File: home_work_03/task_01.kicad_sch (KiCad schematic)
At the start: 29 parts

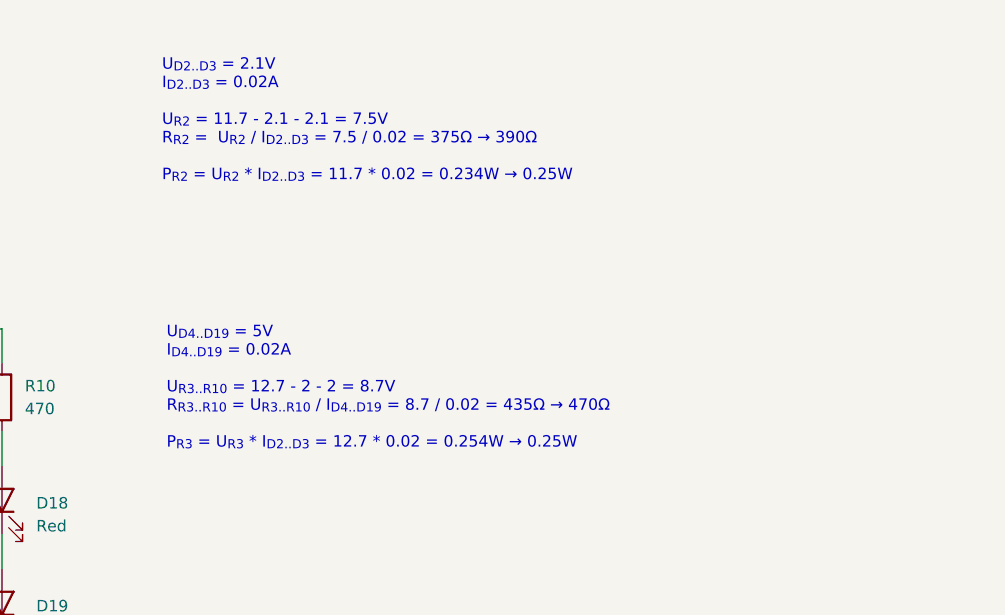
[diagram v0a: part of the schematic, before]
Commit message: fix home work 3
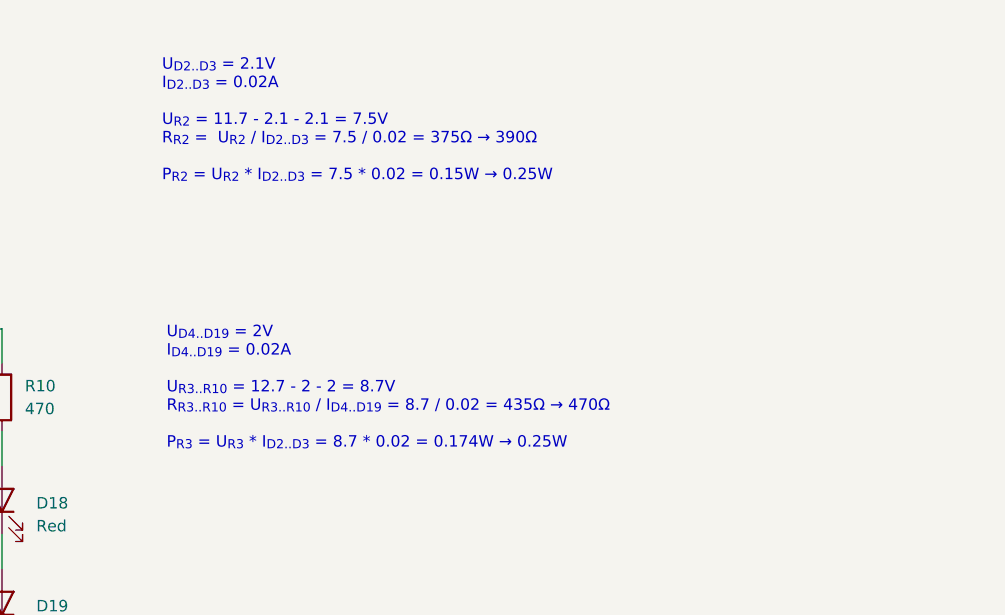
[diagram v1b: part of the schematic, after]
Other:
- note added: "U_{D2..D3} = 2.1V I_{D2..D3} = 0.02A U_{R2} = 11.7 - 2.1 - 2.1 = 7.5V R_{R2} = U_{R2} / I_{D2..D3} = 7.5 / 0.02 = 375Ω → 390Ω P_{R2} = U_{R2} * I_{D2..D3} = 7.5 * 0.02 = 0.15W → 0.25W"
- note added: "U_{D4..D19} = 2V I_{D4..D19} = 0.02A U_{R3..R10} = 12.7 - 2 - 2 = 8.7V R_{R3..R10} = U_{R3..R10} / I_{D4..D19} = 8.7 / 0.02 = 435Ω → 470Ω P_{R3} = U_{R3} * I_{D2..D3} = 8.7 * 0.02 = 0.174W → 0.25W"
- note removed: "U_{D2..D3} = 2.1V I_{D2..D3} = 0.02A U_{R2} = 11.7 - 2.1 - 2.1 = 7.5V R_{R2} = U_{R2} / I_{D2..D3} = 7.5 / 0.02 = 375Ω → 390Ω P_{R2} = U_{R2} * I_{D2..D3} = 11.7 * 0.02 = 0.234W → 0.25W"
- note removed: "U_{D4..D19} = 5V I_{D4..D19} = 0.02A U_{R3..R10} = 12.7 - 2 - 2 = 8.7V R_{R3..R10} = U_{R3..R10} / I_{D4..D19} = 8.7 / 0.02 = 435Ω → 470Ω P_{R3} = U_{R3} * I_{D2..D3} = 12.7 * 0.02 = 0.254W → 0.25W"
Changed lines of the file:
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@@
 		)
 	)
-	(text "U_{D2..D3} = 2.1V\nI_{D2..D3} = 0.02A\n\nU_{R2} = 11.7 - 2.1 - 2.1 = 7.5V\nR_{R2} =  U_{R2} / I_{D2..D3} = 7.5 / 0.02 = 375Ω → 390Ω\n\nP_{R2} = U_{R2} * I_{D2..D3} = 11.7 * 0.02 = 0.234W → 0.25W"
+	(text "U_{D2..D3} = 2.1V\nI_{D2..D3} = 0.02A\n\nU_{R2} = 11.7 - 2.1 - 2.1 = 7.5V\nR_{R2} =  U_{R2} / I_{D2..D3} = 7.5 / 0.02 = 375Ω → 390Ω\n\nP_{R2} = U_{R2} * I_{D2..D3} = 7.5 * 0.02 = 0.15W → 0.25W"
 		(exclude_from_sim no)
 		(at 119.38 74.676 0)
@@
 		)
 	)
-	(text "U_{D4..D19} = 5V\nI_{D4..D19} = 0.02A\n\nU_{R3..R10} = 12.7 - 2 - 2 = 8.7V\nR_{R3..R10} = U_{R3..R10} / I_{D4..D19} = 8.7 / 0.02 = 435Ω → 470Ω\n\nP_{R3} = U_{R3} * I_{D2..D3} = 12.7 * 0.02 = 0.254W → 0.25W"
+	(text "U_{D4..D19} = 2V\nI_{D4..D19} = 0.02A\n\nU_{R3..R10} = 12.7 - 2 - 2 = 8.7V\nR_{R3..R10} = U_{R3..R10} / I_{D4..D19} = 8.7 / 0.02 = 435Ω → 470Ω\n\nP_{R3} = U_{R3} * I_{D2..D3} = 8.7 * 0.02 = 0.174W → 0.25W"
 		(exclude_from_sim no)
 		(at 119.888 104.394 0)

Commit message: fix home work 03
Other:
- note added: "U_{D1} = 3.2V I_{D1} = 0.02A U_{R1} = 7.4 - 3.2 = 4.2V R_{R1} = U_{R1} / I_{D1} = 4.2 / 0.02 = 210Ω → 220Ω P_{R1} = U_{R1} * I_{D1} = 4.2 * 0.02 = 0.084W → 0.125W или 0603"
- note removed: "U_{D1} = 3.2V I_{D1} = 0.05A U_{R1} = 7.4 - 3.2 = 4.2V R_{R1} = U_{R1} / I_{D1} = 4.2 / 0.02 = 210Ω → 220Ω P_{R1} = U_{R1} * I_{D1} = 4.2 * 0.02 = 0.084W → 0.125W или 0603"
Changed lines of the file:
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@@
 		)
 	)
-	(text "U_{D1} = 3.2V\nI_{D1} = 0.05A\n\nU_{R1} = 7.4 - 3.2 = 4.2V\nR_{R1} = U_{R1} / I_{D1} = 4.2 / 0.02 = 210Ω → 220Ω\n\nP_{R1} = U_{R1} * I_{D1} = 4.2 * 0.02 = 0.084W → 0.125W или 0603 "
+	(text "U_{D1} = 3.2V\nI_{D1} = 0.02A\n\nU_{R1} = 7.4 - 3.2 = 4.2V\nR_{R1} = U_{R1} / I_{D1} = 4.2 / 0.02 = 210Ω → 220Ω\n\nP_{R1} = U_{R1} * I_{D1} = 4.2 * 0.02 = 0.084W → 0.125W или 0603 "
 		(exclude_from_sim no)
 		(at 119.634 50.292 0)

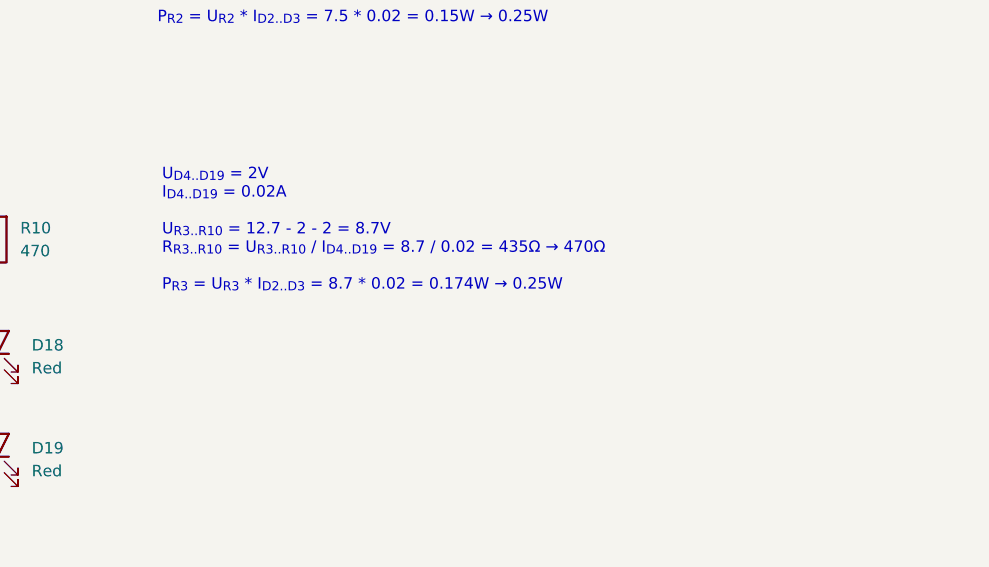
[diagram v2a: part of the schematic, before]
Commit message: fix home work 3
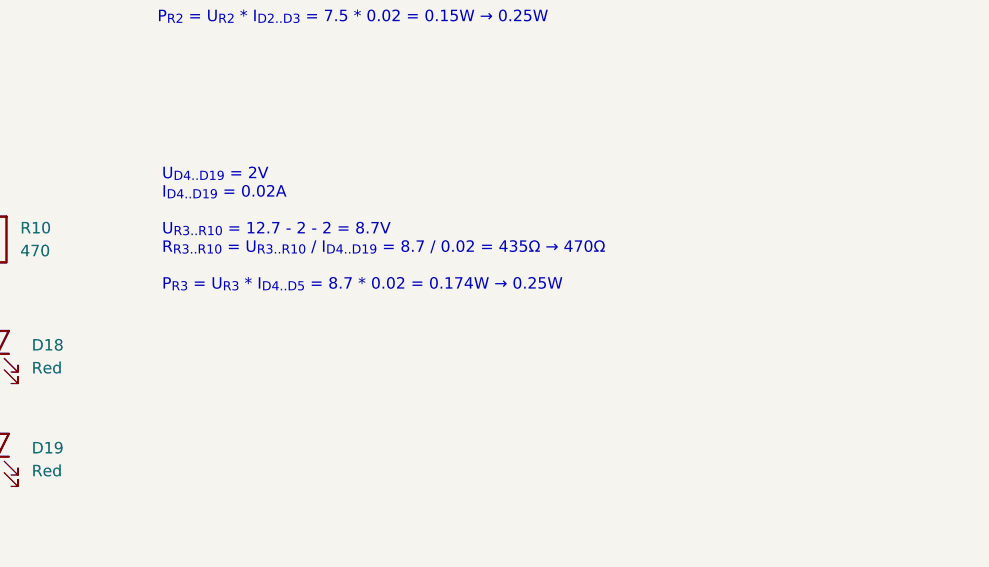
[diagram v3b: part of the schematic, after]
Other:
- note added: "U_{D4..D19} = 2V I_{D4..D19} = 0.02A U_{R3..R10} = 12.7 - 2 - 2 = 8.7V R_{R3..R10} = U_{R3..R10} / I_{D4..D19} = 8.7 / 0.02 = 435Ω → 470Ω P_{R3} = U_{R3} * I_{D4..D5} = 8.7 * 0.02 = 0.174W → 0.25W"
- note removed: "U_{D4..D19} = 2V I_{D4..D19} = 0.02A U_{R3..R10} = 12.7 - 2 - 2 = 8.7V R_{R3..R10} = U_{R3..R10} / I_{D4..D19} = 8.7 / 0.02 = 435Ω → 470Ω P_{R3} = U_{R3} * I_{D2..D3} = 8.7 * 0.02 = 0.174W → 0.25W"
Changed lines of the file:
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@@
 		)
 	)
-	(text "U_{D4..D19} = 2V\nI_{D4..D19} = 0.02A\n\nU_{R3..R10} = 12.7 - 2 - 2 = 8.7V\nR_{R3..R10} = U_{R3..R10} / I_{D4..D19} = 8.7 / 0.02 = 435Ω → 470Ω\n\nP_{R3} = U_{R3} * I_{D2..D3} = 8.7 * 0.02 = 0.174W → 0.25W"
+	(text "U_{D4..D19} = 2V\nI_{D4..D19} = 0.02A\n\nU_{R3..R10} = 12.7 - 2 - 2 = 8.7V\nR_{R3..R10} = U_{R3..R10} / I_{D4..D19} = 8.7 / 0.02 = 435Ω → 470Ω\n\nP_{R3} = U_{R3} * I_{D4..D5} = 8.7 * 0.02 = 0.174W → 0.25W"
 		(exclude_from_sim no)
 		(at 119.888 104.394 0)
@@
 				)
 			)
+			(project "home_work"
+				(path "/69d67e86-2d0f-4caa-88ab-0139115a92ca/91a3f542-ae8f-492d-b48c-64c20e4235c8"
+					(reference "#PWR?")
+					(unit 1)
+				)
+			)
 		)
 	)
@@
 				)
 			)
+			(project "home_work"
+				(path "/69d67e86-2d0f-4caa-88ab-0139115a92ca/91a3f542-ae8f-492d-b48c-64c20e4235c8"
+					(reference "#PWR?")
+					(unit 1)
+				)
+			)
 		)
 	)
@@
 				)
 			)
+			(project "home_work"
+				(path "/69d67e86-2d0f-4caa-88ab-0139115a92ca/91a3f542-ae8f-492d-b48c-64c20e4235c8"
+					(reference "D13")
+					(unit 1)
+				)
+			)
 		)
 	)
@@
 				)
 			)
+			(project "home_work"
+				(path "/69d67e86-2d0f-4caa-88ab-0139115a92ca/91a3f542-ae8f-492d-b48c-64c20e4235c8"
+					(reference "D5")
+					(unit 1)
+				)
+			)
 		)
 	)
@@
 				)
 			)
+			(project "home_work"
+				(path "/69d67e86-2d0f-4caa-88ab-0139115a92ca/91a3f542-ae8f-492d-b48c-64c20e4235c8"
+					(reference "R4")
+					(unit 1)
+				)
+			)
 		)
 	)
@@
 				)
 			)
+			(project "home_work"
+				(path "/69d67e86-2d0f-4caa-88ab-0139115a92ca/91a3f542-ae8f-492d-b48c-64c20e4235c8"
+					(reference "#PWR?")
+					(unit 1)
+				)
+			)
 		)
 	)
@@
 				)
 			)
+			(project "home_work"
+				(path "/69d67e86-2d0f-4caa-88ab-0139115a92ca/91a3f542-ae8f-492d-b48c-64c20e4235c8"
+					(reference "R6")
+					(unit 1)
+				)
+			)
 		)
 	)
@@
 				)
 			)
+			(project "home_work"
+				(path "/69d67e86-2d0f-4caa-88ab-0139115a92ca/91a3f542-ae8f-492d-b48c-64c20e4235c8"
+					(reference "#PWR?")
+					(unit 1)
+				)
+			)
 		)
 	)
@@
 				)
 			)
+			(project "home_work"
+				(path "/69d67e86-2d0f-4caa-88ab-0139115a92ca/91a3f542-ae8f-492d-b48c-64c20e4235c8"
+					(reference "R8")
+					(unit 1)
+				)
+			)
 		)
 	)
@@
 				)
 			)
+			(project "home_work"
+				(path "/69d67e86-2d0f-4caa-88ab-0139115a92ca/91a3f542-ae8f-492d-b48c-64c20e4235c8"
+					(reference "D19")
+					(unit 1)
+				)
+			)
 		)
 	)
@@
 				)
 			)
+			(project "home_work"
+				(path "/69d67e86-2d0f-4caa-88ab-0139115a92ca/91a3f542-ae8f-492d-b48c-64c20e4235c8"
+					(reference "D1")
+					(unit 1)
+				)
+			)
 		)
 	)
@@
 				)
 			)
+			(project "home_work"
+				(path "/69d67e86-2d0f-4caa-88ab-0139115a92ca/91a3f542-ae8f-492d-b48c-64c20e4235c8"
+					(reference "R3")
+					(unit 1)
+				)
+			)
 		)
 	)
@@
 				)
 			)
+			(project "home_work"
+				(path "/69d67e86-2d0f-4caa-88ab-0139115a92ca/91a3f542-ae8f-492d-b48c-64c20e4235c8"
+					(reference "R9")
+					(unit 1)
+				)
+			)
 		)
 	)
@@
 				)
 			)
+			(project "home_work"
+				(path "/69d67e86-2d0f-4caa-88ab-0139115a92ca/91a3f542-ae8f-492d-b48c-64c20e4235c8"
+					(reference "D8")
+					(unit 1)
+				)
+			)
 		)
 	)
@@
 				)
 			)
+			(project "home_work"
+				(path "/69d67e86-2d0f-4caa-88ab-0139115a92ca/91a3f542-ae8f-492d-b48c-64c20e4235c8"
+					(reference "D9")
+					(unit 1)
+				)
+			)
 		)
 	)
@@
 				)
 			)
+			(project "home_work"
+				(path "/69d67e86-2d0f-4caa-88ab-0139115a92ca/91a3f542-ae8f-492d-b48c-64c20e4235c8"
+					(reference "R7")
+					(unit 1)
+				)
+			)
 		)
 	)
@@
 				)
 			)
+			(project "home_work"
+				(path "/69d67e86-2d0f-4caa-88ab-0139115a92ca/91a3f542-ae8f-492d-b48c-64c20e4235c8"
+					(reference "#PWR?")
+					(unit 1)
+				)
+			)
 		)
 	)
@@
 				)
 			)
+			(project "home_work"
+				(path "/69d67e86-2d0f-4caa-88ab-0139115a92ca/91a3f542-ae8f-492d-b48c-64c20e4235c8"
+					(reference "R1")
+					(unit 1)
+				)
+			)
 		)
 	)
@@
 				)
 			)
+			(project "home_work"
+				(path "/69d67e86-2d0f-4caa-88ab-0139115a92ca/91a3f542-ae8f-492d-b48c-64c20e4235c8"
+					(reference "D3")
+					(unit 1)
+				)
+			)
 		)
 	)
@@
 				)
 			)
+			(project "home_work"
+				(path "/69d67e86-2d0f-4caa-88ab-0139115a92ca/91a3f542-ae8f-492d-b48c-64c20e4235c8"
+					(reference "D7")
+					(unit 1)
+				)
+			)
 		)
 	)
@@
 				)
 			)
+			(project "home_work"
+				(path "/69d67e86-2d0f-4caa-88ab-0139115a92ca/91a3f542-ae8f-492d-b48c-64c20e4235c8"
+					(reference "D10")
+					(unit 1)
+				)
+			)
 		)
 	)
@@
 				)
 			)
+			(project "home_work"
+				(path "/69d67e86-2d0f-4caa-88ab-0139115a92ca/91a3f542-ae8f-492d-b48c-64c20e4235c8"
+					(reference "D17")
+					(unit 1)
+				)
+			)
 		)
 	)
@@
 				)
 			)
+			(project "home_work"
+				(path "/69d67e86-2d0f-4caa-88ab-0139115a92ca/91a3f542-ae8f-492d-b48c-64c20e4235c8"
+					(reference "R2")
+					(unit 1)
+				)
+			)
 		)
 	)
@@
 				)
 			)
+			(project "home_work"
+				(path "/69d67e86-2d0f-4caa-88ab-0139115a92ca/91a3f542-ae8f-492d-b48c-64c20e4235c8"
+					(reference "D15")
+					(unit 1)
+				)
+			)
 		)
 	)
@@
 				)
 			)
+			(project "home_work"
+				(path "/69d67e86-2d0f-4caa-88ab-0139115a92ca/91a3f542-ae8f-492d-b48c-64c20e4235c8"
+					(reference "D18")
+					(unit 1)
+				)
+			)
 		)
 	)
@@
 				)
 			)
+			(project "home_work"
+				(path "/69d67e86-2d0f-4caa-88ab-0139115a92ca/91a3f542-ae8f-492d-b48c-64c20e4235c8"
+					(reference "R5")
+					(unit 1)
+				)
+			)
 		)
 	)
@@
 				)
 			)
+			(project "home_work"
+				(path "/69d67e86-2d0f-4caa-88ab-0139115a92ca/91a3f542-ae8f-492d-b48c-64c20e4235c8"
+					(reference "D16")
+					(unit 1)
+				)
+			)
 		)
 	)
@@
 				)
 			)
+			(project "home_work"
+				(path "/69d67e86-2d0f-4caa-88ab-0139115a92ca/91a3f542-ae8f-492d-b48c-64c20e4235c8"
+					(reference "D11")
+					(unit 1)
+				)
+			)
 		)
 	)
@@
 				)
 			)
+			(project "home_work"
+				(path "/69d67e86-2d0f-4caa-88ab-0139115a92ca/91a3f542-ae8f-492d-b48c-64c20e4235c8"
+					(reference "R10")
+					(unit 1)
+				)
+			)
 		)
 	)
@@
 				)
 			)
+			(project "home_work"
+				(path "/69d67e86-2d0f-4caa-88ab-0139115a92ca/91a3f542-ae8f-492d-b48c-64c20e4235c8"
+					(reference "D2")
+					(unit 1)
+				)
+			)
 		)
 	)
@@
 				)
 			)
+			(project "home_work"
+				(path "/69d67e86-2d0f-4caa-88ab-0139115a92ca/91a3f542-ae8f-492d-b48c-64c20e4235c8"
+					(reference "D12")
+					(unit 1)
+				)
+			)
 		)
 	)
@@
 				)
 			)
+			(project "home_work"
+				(path "/69d67e86-2d0f-4caa-88ab-0139115a92ca/91a3f542-ae8f-492d-b48c-64c20e4235c8"
+					(reference "D14")
+					(unit 1)
+				)
+			)
 		)
 	)
@@
 				)
 			)
+			(project "home_work"
+				(path "/69d67e86-2d0f-4caa-88ab-0139115a92ca/91a3f542-ae8f-492d-b48c-64c20e4235c8"
+					(reference "#PWR?")
+					(unit 1)
+				)
+			)
 		)
 	)
@@
 				)
 			)
+			(project "home_work"
+				(path "/69d67e86-2d0f-4caa-88ab-0139115a92ca/91a3f542-ae8f-492d-b48c-64c20e4235c8"
+					(reference "D4")
+					(unit 1)
+				)
+			)
 		)
 	)
@@
 					(reference "D6")
 					(unit 1)
+				)
+			)
+			(project "home_work"
+				(path "/69d67e86-2d0f-4caa-88ab-0139115a92ca/91a3f542-ae8f-492d-b48c-64c20e4235c8"
+					(reference "D6")
+					(unit 1)
